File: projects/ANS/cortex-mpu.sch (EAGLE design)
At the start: 74 parts, among them IC1 LM1117MPX-3.3, U1 AT32UC3B164-AUT, Y1 7A-16

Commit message: Decoupling, MPU
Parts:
- removed C1, C2, C3, C5: 2.7nF, SparkFun-Passives:CAP0603-CAP
- removed C10, C12, C13, C15, C17, C21, C26, C8: 100nF, SparkFun-Passives:CAP0603-CAP
- removed C11, C14, C16, C18, C23, C25, C4, C7, C9: 33nF, SparkFun-Passives:CAP0603-CAP
- removed C19, C22: 2.2uF, SparkFun-Passives:CAP0603-CAP
- removed C20: 4.7uF, SparkFun-Passives:CAP0603-CAP
- removed C24: 470pF, SparkFun-Passives:CAP0603-CAP
- removed C6: 2.2nF, SparkFun-Passives:CAP0603-CAP
- added C38, C39, C40, C41, C42, C43, C44: 100nF, SparkFun-Passives:CAP0603-CAP
- added C45, C46, C47, C48, C49, C50, C51: (no value), SparkFun-Passives:CAP0603-CAP
- added JP3: (no value), SparkFun-Connectors:M02LOCK
- added PA21, PA22, PA3, PA4: (no value), wirepad:1,6/0,8
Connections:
- removed net V33: C36.1, IC1.OUT, IC1.OUT1
- removed net VDDCORE: C1.1, C11.1, C13.1, C15.1, C17.1, C19.1, C3.1, C5.1, C7.1, C9.1
- removed net VDDIO: C10.1, C12.1, C14.1, C16.1, C18.1, C20.1, C8.1
- new net ADVREF: C50.1, C51.1, U1.ADVREF
- new net VDDCORE0: C38.1, U1.VDDCORE
- new net VDDCORE1: C39.1, U1.VDDCORE_2
- new net VDDCORE2: C40.1, U1.VDDCORE_3
- new net VDDIO0: C42.1, U1.VDDIO
- new net VDDIO1: C43.1, U1.VDDIO_2
- new net VDDIO2: C44.1, U1.VDDIO_3
- net GND: now also C38.2, C39.2, C40.2, C41.2, C42.2, C43.2, C44.2, C45.2, C46.2, C47.2, C48.2, C49.2, C50.2, C51.2, JP3.2; no longer C1.2, C10.2, C11.2, C12.2, C13.2, C14.2, C15.2, C16.2, C17.2, C18.2, C19.2, C2.2, C20.2, C21.2, C22.2, C23.2, C24.2, C25.2, C26.2, C3.2, C4.2, C5.2, C6.2, C7.2, C8.2, C9.2
- net PA21: now also PA21.P
- net PA22: now also PA22.P
- net PA3: now also PA3.P
- net PA4: now also PA4.P
- net VBUS: now also JP3.1
- net VCC: now also C36.1, IC1.OUT, IC1.OUT1; no longer U1.ADVREF, U1.VDDANA, U1.VDDIN, U1.VDDIO, U1.VDDIO_2, U1.VDDIO_3
- net VDDANA: now also C45.1, U1.VDDANA; no longer C21.1, C23.1
- net VDDIN: now also C46.1, C47.1, U1.VDDIN; no longer C25.1, C26.1
- net VDDOUT: now also C48.1, C49.1, U1.VDDOUT; no longer C22.1, C24.1
- net VDDPLL: now also C41.1; no longer C2.1, C4.1, C6.1, U1.VDDCORE, U1.VDDCORE_2, U1.VDDCORE_3, U1.VDDOUT
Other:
- note added: "ADC PWM"
- note added: "V(in)"
- moved on the sheet: SJ3, U1

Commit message: Power conn
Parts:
- added SJ4, SJ5, SJ6, SJ7: JUMPER-PAD-2-NC_BY_TRACE, SparkFun-Passives:JUMPER-PAD-2-NC_BY_TRACE
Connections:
- net VDDCORE0: now also SJ4.1
- net VDDCORE1: now also SJ5.1
- net VDDCORE2: now also SJ6.1
- net VDDOUT: now also SJ4.2, SJ5.2, SJ6.2, SJ7.2
- net VDDPLL: now also SJ7.1
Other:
- note added: "Power"
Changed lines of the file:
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@@
 <part name="PA4" library="wirepad" deviceset="1,6/0,8" device=""/>
 <part name="PA21" library="wirepad" deviceset="1,6/0,8" device=""/>
+<part name="SUPPLY7" library="SparkFun-Aesthetics" deviceset="VCC" device=""/>
+<part name="SUPPLY8" library="SparkFun-Aesthetics" deviceset="VCC" device=""/>
+<part name="SUPPLY9" library="SparkFun-Aesthetics" deviceset="VCC" device=""/>
+<part name="SUPPLY10" library="SparkFun-Aesthetics" deviceset="VCC" device=""/>
+<part name="SUPPLY11" library="SparkFun-Aesthetics" deviceset="VCC" device=""/>
+<part name="SUPPLY12" library="SparkFun-Aesthetics" deviceset="VCC" device=""/>
+<part name="SJ4" library="SparkFun-Passives" deviceset="JUMPER-PAD-2-NC_BY_TRACE" device="" value=""/>
+<part name="SJ5" library="SparkFun-Passives" deviceset="JUMPER-PAD-2-NC_BY_TRACE" device="" value=""/>
+<part name="SJ6" library="SparkFun-Passives" deviceset="JUMPER-PAD-2-NC_BY_TRACE" device="" value=""/>
+<part name="SJ7" library="SparkFun-Passives" deviceset="JUMPER-PAD-2-NC_BY_TRACE" device="" value=""/>
 </parts>
 <sheets>
@@
 <wire x1="5.08" y1="63.5" x2="96.52" y2="63.5" width="0.1524" layer="95"/>
 <wire x1="96.52" y1="63.5" x2="96.52" y2="170.18" width="0.1524" layer="95"/>
+<text x="35.56" y="58.42" size="2.54" layer="95" align="center">Power</text>
+<wire x1="96.52" y1="60.96" x2="96.52" y2="35.56" width="0.1524" layer="95"/>
+<wire x1="96.52" y1="35.56" x2="27.94" y2="35.56" width="0.1524" layer="95"/>
+<wire x1="27.94" y1="35.56" x2="27.94" y2="60.96" width="0.1524" layer="95"/>
+<wire x1="27.94" y1="60.96" x2="96.52" y2="60.96" width="0.1524" layer="95"/>
 </plain>
 <instances>
@@
 <instance part="PA4" gate="P" x="116.84" y="48.26" rot="R270"/>
 <instance part="PA21" gate="P" x="101.6" y="48.26" rot="R270"/>
+<instance part="SUPPLY7" gate="G$1" x="30.48" y="48.26"/>
+<instance part="SUPPLY8" gate="G$1" x="35.56" y="48.26"/>
+<instance part="SUPPLY9" gate="G$1" x="40.64" y="48.26"/>
+<instance part="SUPPLY10" gate="G$1" x="45.72" y="48.26"/>
+<instance part="SUPPLY11" gate="G$1" x="50.8" y="48.26"/>
+<instance part="SUPPLY12" gate="G$1" x="55.88" y="48.26"/>
+<instance part="SJ4" gate="G$1" x="68.58" y="48.26" rot="R90"/>
+<instance part="SJ5" gate="G$1" x="73.66" y="48.26" rot="R90"/>
+<instance part="SJ6" gate="G$1" x="78.74" y="48.26" rot="R90"/>
+<instance part="SJ7" gate="G$1" x="83.82" y="48.26" rot="R90"/>
 </instances>
 <busses>
@@
 <label x="12.7" y="154.94" size="1.778" layer="95"/>
 </segment>
+<segment>
+<pinref part="SUPPLY7" gate="G$1" pin="VCC"/>
+<wire x1="30.48" y1="48.26" x2="30.48" y2="40.64" width="0.1524" layer="91"/>
+<label x="30.48" y="38.1" size="1.778" layer="95"/>
+</segment>
 </net>
 <net name="VDDIN" class="0">
@@
 <label x="12.7" y="144.78" size="1.778" layer="95"/>
 </segment>
+<segment>
+<pinref part="SUPPLY8" gate="G$1" pin="VCC"/>
+<wire x1="35.56" y1="48.26" x2="35.56" y2="43.18" width="0.1524" layer="91"/>
+<label x="35.56" y="40.64" size="1.778" layer="95"/>
+</segment>
 </net>
 <net name="VDDOUT" class="0">
@@
 <label x="12.7" y="134.62" size="1.778" layer="95"/>
 </segment>
+<segment>
+<pinref part="SJ4" gate="G$1" pin="2"/>
+<wire x1="68.58" y1="53.34" x2="68.58" y2="55.88" width="0.1524" layer="91"/>
+<wire x1="68.58" y1="55.88" x2="73.66" y2="55.88" width="0.1524" layer="91"/>
+<pinref part="SJ6" gate="G$1" pin="2"/>
+<wire x1="73.66" y1="55.88" x2="76.2" y2="55.88" width="0.1524" layer="91"/>
+<wire x1="76.2" y1="55.88" x2="78.74" y2="55.88" width="0.1524" layer="91"/>
+<wire x1="78.74" y1="55.88" x2="78.74" y2="53.34" width="0.1524" layer="91"/>
+<pinref part="SJ5" gate="G$1" pin="2"/>
+<wire x1="73.66" y1="53.34" x2="73.66" y2="55.88" width="0.1524" layer="91"/>
+<junction x="73.66" y="55.88"/>
+<wire x1="78.74" y1="55.88" x2="83.82" y2="55.88" width="0.1524" layer="91"/>
+<junction x="78.74" y="55.88"/>
+<pinref part="SJ7" gate="G$1" pin="2"/>
+<wire x1="83.82" y1="55.88" x2="83.82" y2="53.34" width="0.1524" layer="91"/>
+<wire x1="76.2" y1="55.88" x2="76.2" y2="58.42" width="0.1524" layer="91"/>
+<junction x="76.2" y="55.88"/>
+<label x="76.2" y="58.42" size="1.778" layer="95"/>
+</segment>
 </net>
 <net name="VDDPLL" class="0">
@@
 <wire x1="27.94" y1="132.08" x2="22.86" y2="132.08" width="0.1524" layer="91"/>
 <label x="12.7" y="132.08" size="1.778" layer="95"/>
+</segment>
+<segment>
+<pinref part="SJ7" gate="G$1" pin="1"/>
+<wire x1="83.82" y1="43.18" x2="83.82" y2="38.1" width="0.1524" layer="91"/>
+<label x="83.82" y="40.64" size="1.778" layer="95"/>
 </segment>
 </net>
@@
 <label x="12.7" y="149.86" size="1.778" layer="95"/>
 </segment>
+<segment>
+<pinref part="SJ6" gate="G$1" pin="1"/>
+<wire x1="78.74" y1="43.18" x2="78.74" y2="40.64" width="0.1524" layer="91"/>
+<label x="78.74" y="38.1" size="1.778" layer="95"/>
+</segment>
 </net>
 <net name="VDDCORE1" class="0">
@@
 <label x="12.7" y="152.4" size="1.778" layer="95"/>
 </segment>
+<segment>
+<pinref part="SJ5" gate="G$1" pin="1"/>
+<wire x1="73.66" y1="43.18" x2="73.66" y2="40.64" width="0.1524" layer="91"/>
+<label x="71.12" y="40.64" size="1.778" layer="95"/>
+</segment>
 </net>
 <net name="VDDCORE0" class="0">
@@
 <label x="12.7" y="147.32" size="1.778" layer="95"/>
 </segment>
+<segment>
+<pinref part="SJ4" gate="G$1" pin="1"/>
+<wire x1="68.58" y1="43.18" x2="68.58" y2="38.1" width="0.1524" layer="91"/>
+<label x="63.5" y="38.1" size="1.778" layer="95"/>
+</segment>
 </net>
 <net name="VDDIO0" class="0">
@@
 <label x="12.7" y="137.16" size="1.778" layer="95"/>
 </segment>
+<segment>
+<pinref part="SUPPLY10" gate="G$1" pin="VCC"/>
+<wire x1="45.72" y1="48.26" x2="45.72" y2="40.64" width="0.1524" layer="91"/>
+<label x="45.72" y="38.1" size="1.778" layer="95"/>
+</segment>
 </net>
 <net name="VDDIO1" class="0">
@@
 <label x="12.7" y="142.24" size="1.778" layer="95"/>
 </segment>
+<segment>
+<pinref part="SUPPLY11" gate="G$1" pin="VCC"/>
+<wire x1="50.8" y1="48.26" x2="50.8" y2="43.18" width="0.1524" layer="91"/>
+<label x="50.8" y="40.64" size="1.778" layer="95"/>
+</segment>
 </net>
 <net name="VDDIO2" class="0">
@@
 <wire x1="27.94" y1="139.7" x2="22.86" y2="139.7" width="0.1524" layer="91"/>
 <label x="12.7" y="139.7" size="1.778" layer="95"/>
+</segment>
+<segment>
+<pinref part="SUPPLY12" gate="G$1" pin="VCC"/>
+<wire x1="55.88" y1="48.26" x2="55.88" y2="45.72" width="0.1524" layer="91"/>
+<label x="55.88" y="43.18" size="1.778" layer="95"/>
 </segment>
 </net>
@@
 <label x="12.7" y="127" size="1.778" layer="95"/>
 </segment>
-</net>
+<segment>
+<pinref part="SUPPLY9" gate="G$1" pin="VCC"/>
+<wire x1="40.64" y1="48.26" x2="40.64" y2="45.72" width="0.1524" layer="91"/>
+<label x="40.64" y="43.18" size="1.778" layer="95"/>
+</segment>
+</net>

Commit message: Schematics - Done
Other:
- note added: "MCU"
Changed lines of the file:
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@@
 <wire x1="5.08" y1="63.5" x2="96.52" y2="63.5" width="0.1524" layer="95"/>
 <wire x1="96.52" y1="63.5" x2="96.52" y2="170.18" width="0.1524" layer="95"/>
-<text x="35.56" y="58.42" size="2.54" layer="95" align="center">Power</text>
+<text x="15.24" y="58.42" size="2.54" layer="95" rot="R180" align="center">Power</text>
 <wire x1="96.52" y1="60.96" x2="96.52" y2="35.56" width="0.1524" layer="95"/>
-<wire x1="96.52" y1="35.56" x2="27.94" y2="35.56" width="0.1524" layer="95"/>
-<wire x1="27.94" y1="35.56" x2="27.94" y2="60.96" width="0.1524" layer="95"/>
-<wire x1="27.94" y1="60.96" x2="96.52" y2="60.96" width="0.1524" layer="95"/>
+<wire x1="96.52" y1="35.56" x2="5.08" y2="35.56" width="0.1524" layer="95"/>
+<wire x1="5.08" y1="35.56" x2="5.08" y2="60.96" width="0.1524" layer="95"/>
+<wire x1="5.08" y1="60.96" x2="96.52" y2="60.96" width="0.1524" layer="95"/>
+<text x="15.24" y="68.58" size="2.54" layer="95" align="center">MCU</text>
 </plain>
 <instances>
@@
 <instance part="PA4" gate="P" x="116.84" y="48.26" rot="R270"/>
 <instance part="PA21" gate="P" x="101.6" y="48.26" rot="R270"/>
-<instance part="SUPPLY7" gate="G$1" x="30.48" y="48.26"/>
-<instance part="SUPPLY8" gate="G$1" x="35.56" y="48.26"/>
-<instance part="SUPPLY9" gate="G$1" x="40.64" y="48.26"/>
-<instance part="SUPPLY10" gate="G$1" x="45.72" y="48.26"/>
-<instance part="SUPPLY11" gate="G$1" x="50.8" y="48.26"/>
-<instance part="SUPPLY12" gate="G$1" x="55.88" y="48.26"/>
+<instance part="SUPPLY7" gate="G$1" x="17.78" y="48.26"/>
+<instance part="SUPPLY8" gate="G$1" x="22.86" y="48.26"/>
+<instance part="SUPPLY9" gate="G$1" x="27.94" y="48.26"/>
+<instance part="SUPPLY10" gate="G$1" x="33.02" y="48.26"/>
+<instance part="SUPPLY11" gate="G$1" x="38.1" y="48.26"/>
+<instance part="SUPPLY12" gate="G$1" x="43.18" y="48.26"/>
 <instance part="SJ4" gate="G$1" x="68.58" y="48.26" rot="R90"/>
 <instance part="SJ5" gate="G$1" x="73.66" y="48.26" rot="R90"/>
@@
 <segment>
 <pinref part="SUPPLY7" gate="G$1" pin="VCC"/>
-<wire x1="30.48" y1="48.26" x2="30.48" y2="40.64" width="0.1524" layer="91"/>
-<label x="30.48" y="38.1" size="1.778" layer="95"/>
+<wire x1="17.78" y1="48.26" x2="17.78" y2="40.64" width="0.1524" layer="91"/>
+<label x="17.78" y="38.1" size="1.778" layer="95"/>
 </segment>
 </net>
@@
 <segment>
 <pinref part="SUPPLY8" gate="G$1" pin="VCC"/>
-<wire x1="35.56" y1="48.26" x2="35.56" y2="43.18" width="0.1524" layer="91"/>
-<label x="35.56" y="40.64" size="1.778" layer="95"/>
+<wire x1="22.86" y1="48.26" x2="22.86" y2="43.18" width="0.1524" layer="91"/>
+<label x="22.86" y="40.64" size="1.778" layer="95"/>
 </segment>
 </net>
@@
 <segment>
 <pinref part="SUPPLY10" gate="G$1" pin="VCC"/>
-<wire x1="45.72" y1="48.26" x2="45.72" y2="40.64" width="0.1524" layer="91"/>
-<label x="45.72" y="38.1" size="1.778" layer="95"/>
+<wire x1="33.02" y1="48.26" x2="33.02" y2="40.64" width="0.1524" layer="91"/>
+<label x="33.02" y="38.1" size="1.778" layer="95"/>
 </segment>
 </net>
@@
 <segment>
 <pinref part="SUPPLY11" gate="G$1" pin="VCC"/>
-<wire x1="50.8" y1="48.26" x2="50.8" y2="43.18" width="0.1524" layer="91"/>
-<label x="50.8" y="40.64" size="1.778" layer="95"/>
+<wire x1="38.1" y1="48.26" x2="38.1" y2="43.18" width="0.1524" layer="91"/>
+<label x="38.1" y="40.64" size="1.778" layer="95"/>
 </segment>
 </net>
@@
 <segment>
 <pinref part="SUPPLY12" gate="G$1" pin="VCC"/>
-<wire x1="55.88" y1="48.26" x2="55.88" y2="45.72" width="0.1524" layer="91"/>
-<label x="55.88" y="43.18" size="1.778" layer="95"/>
+<wire x1="43.18" y1="48.26" x2="43.18" y2="45.72" width="0.1524" layer="91"/>
+<label x="43.18" y="43.18" size="1.778" layer="95"/>
 </segment>
 </net>
@@
 <segment>
 <pinref part="SUPPLY9" gate="G$1" pin="VCC"/>
-<wire x1="40.64" y1="48.26" x2="40.64" y2="45.72" width="0.1524" layer="91"/>
-<label x="40.64" y="43.18" size="1.778" layer="95"/>
-</segment>
-</net>
+<wire x1="27.94" y1="48.26" x2="27.94" y2="45.72" width="0.1524" layer="91"/>
+<label x="27.94" y="43.18" size="1.778" layer="95"/>
+</segment>
+</net>

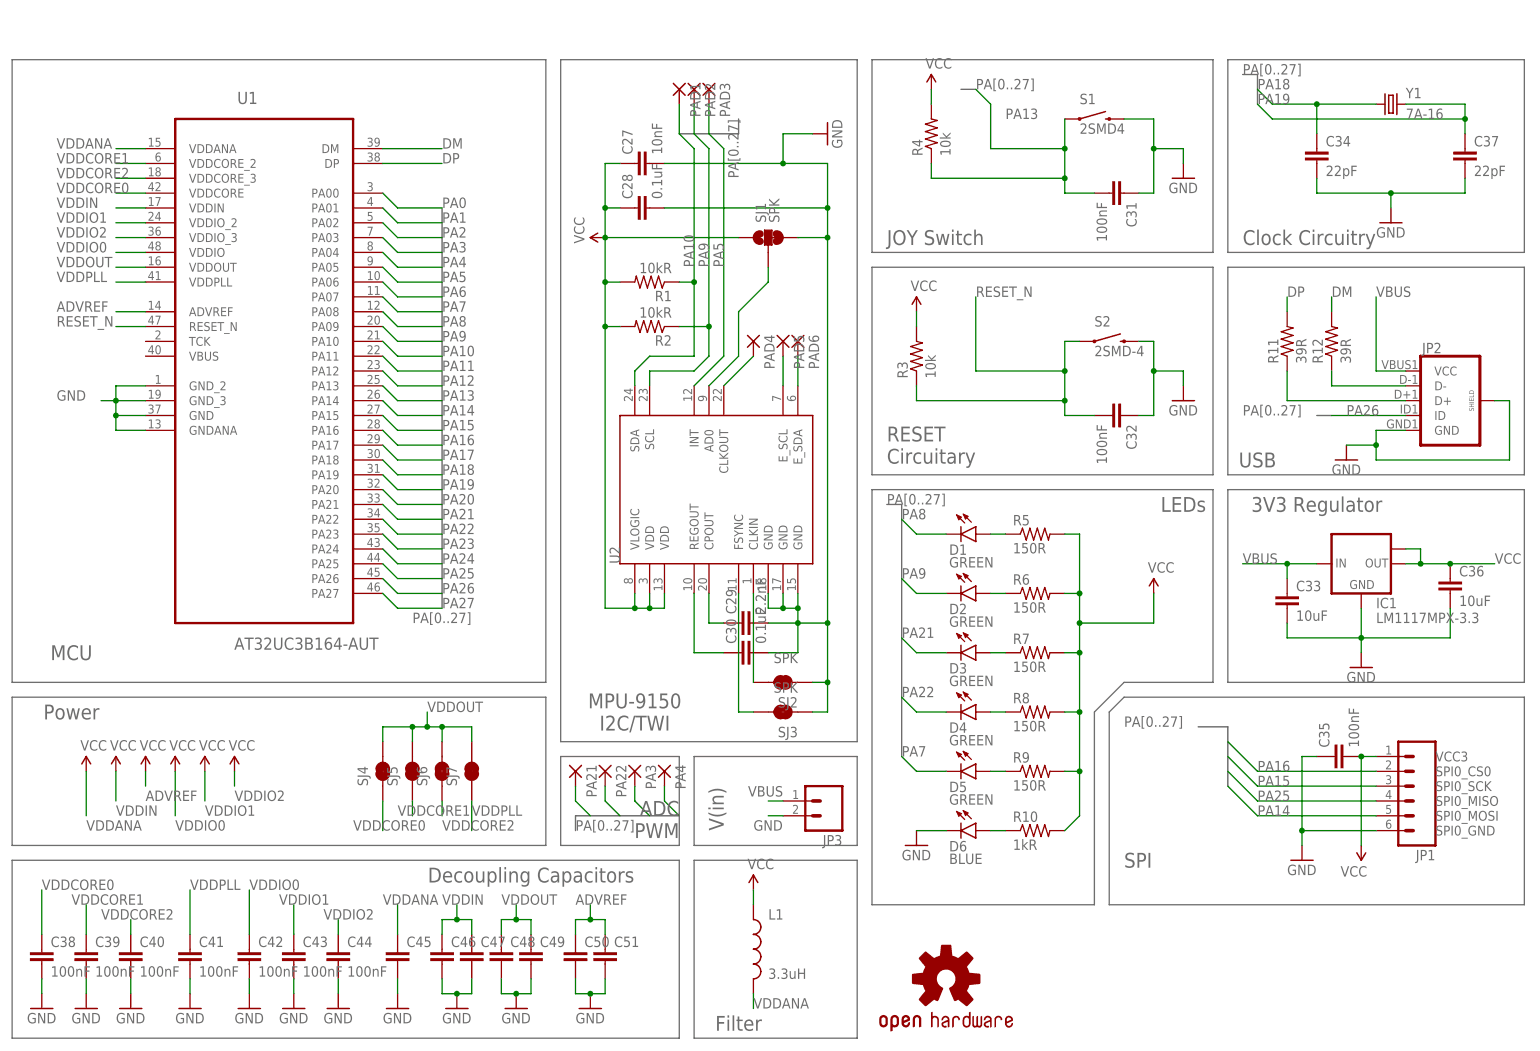
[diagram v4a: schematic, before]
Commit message: Shematics, purged unneded files
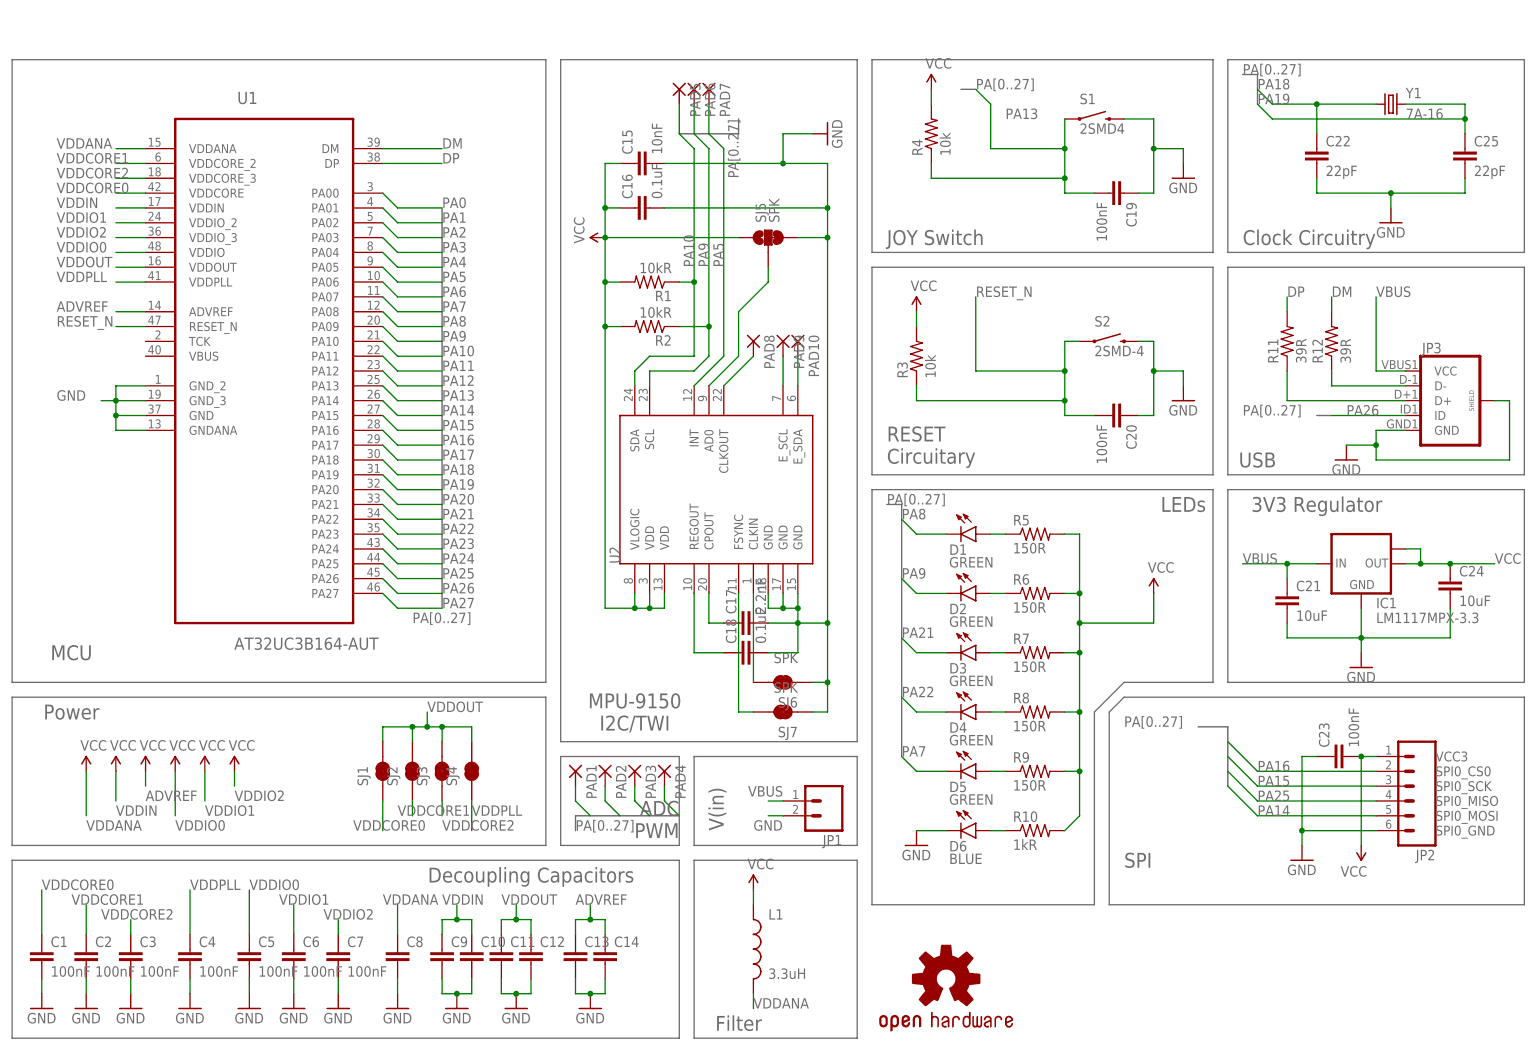
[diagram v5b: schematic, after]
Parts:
- removed PA21, PA22, PA3, PA4: (no value), wirepad:1,6/0,8
- added PAD10, PAD7, PAD8, PAD9: (no value), wirepad:1,6/0,8
- JP1: device SparkFun-Connectors:M06LOCK_LONGPADS -> SparkFun-Connectors:M02LOCK
- JP2: device SparkFun-Connectors:USB_MICROB_PLUGCONN-11752 -> SparkFun-Connectors:M06LOCK_LONGPADS
- JP3: device SparkFun-Connectors:M02LOCK -> SparkFun-Connectors:USB_MICROB_PLUGCONN-11752
- SJ1: value SPK -> JUMPER-PAD-2-NC_BY_TRACE; device SparkFun-Passives:JUMPER-PAD-3-2OF3_NC_BY_TRACE_LARGE -> SparkFun-Passives:JUMPER-PAD-2-NC_BY_TRACE
- SJ2, SJ3: value SPK -> JUMPER-PAD-2-NC_BY_TRACE
- SJ5: value JUMPER-PAD-2-NC_BY_TRACE -> SPK; device SparkFun-Passives:JUMPER-PAD-2-NC_BY_TRACE -> SparkFun-Passives:JUMPER-PAD-3-2OF3_NC_BY_TRACE_LARGE
- SJ6, SJ7: value JUMPER-PAD-2-NC_BY_TRACE -> SPK
- renumbered C27 to C15, C28 to C16, C29 to C17, C30 to C18, C31 to C19, C32 to C20, C33 to C21, C34 to C22, C35 to C23, C36 to C24, C37 to C25, C38 to C1, C39 to C2, C40 to C3, C41 to C4, C42 to C5, C43 to C6, C44 to C7, C45 to C8, C46 to C9, C47 to C10, C48 to C11, C49 to C12, C50 to C13, C51 to C14
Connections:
- net E_SDA: now also PAD10.P; no longer PAD6.P
- net GND: now also JP1.2, JP2.6, JP3.GND, JP3.SHIELD, SJ5.3, SJ6.1, SJ7.1; no longer JP1.6, JP2.GND, JP2.SHIELD, JP3.2, SJ1.3, SJ2.1, SJ3.1
- net N$1: now also JP3.D-; no longer JP2.D-
- net N$12: now also SJ5.2; no longer SJ1.2
- net N$14: now also PAD9.P; no longer PAD5.P
- net N$15: now also SJ7.2; no longer SJ3.2
- net N$16: now also PAD8.P; no longer PAD4.P
- net N$2: now also JP3.D+; no longer JP2.D+
- net N$9: now also SJ6.2; no longer SJ2.2
- net PA10: now also PAD5.P; no longer PAD1.P
- net PA14: now also JP2.5; no longer JP1.5
- net PA15: now also JP2.3; no longer JP1.3
- net PA16: now also JP2.2; no longer JP1.2
- net PA21: now also PAD1.P; no longer PA21.P
- net PA22: now also PAD2.P; no longer PA22.P
- net PA25: now also JP2.4; no longer JP1.4
- net PA26: now also JP3.ID; no longer JP2.ID
- net PA3: now also PAD3.P; no longer PA3.P
- net PA4: now also PAD4.P; no longer PA4.P
- net PA5: now also PAD7.P; no longer PAD3.P
- net PA9: now also PAD6.P; no longer PAD2.P
- net VBUS: now also JP1.1, JP3.VCC; no longer JP2.VCC, JP3.1
- net VCC: now also JP2.1, SJ5.1; no longer JP1.1, SJ1.1
- net VDDCORE0: now also SJ1.1; no longer SJ4.1
- net VDDCORE1: now also SJ2.1; no longer SJ5.1
- net VDDCORE2: now also SJ3.1; no longer SJ6.1
- net VDDOUT: now also SJ1.2, SJ2.2, SJ3.2; no longer SJ5.2, SJ6.2, SJ7.2
- net VDDPLL: now also SJ4.1; no longer SJ7.1
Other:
- moved on the sheet: PAD1, PAD2, PAD3, PAD4, PAD5, PAD6, SJ2, SJ3, SJ4, SJ6, SJ7
